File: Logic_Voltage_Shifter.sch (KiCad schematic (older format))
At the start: 5 parts, among them U5 TXB0104

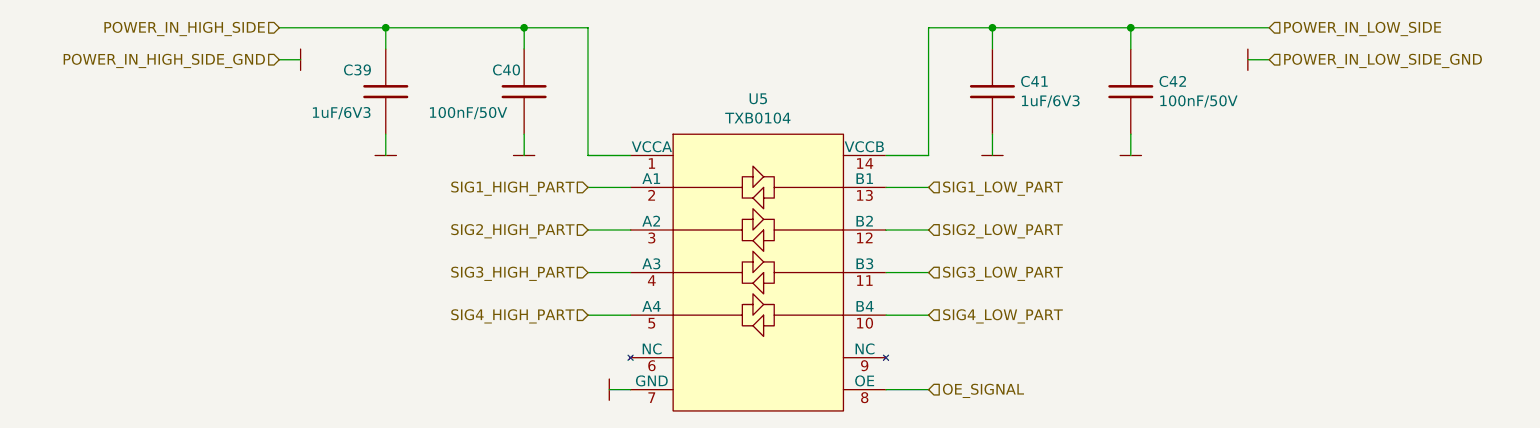
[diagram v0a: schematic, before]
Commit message: Continue connections on schematic
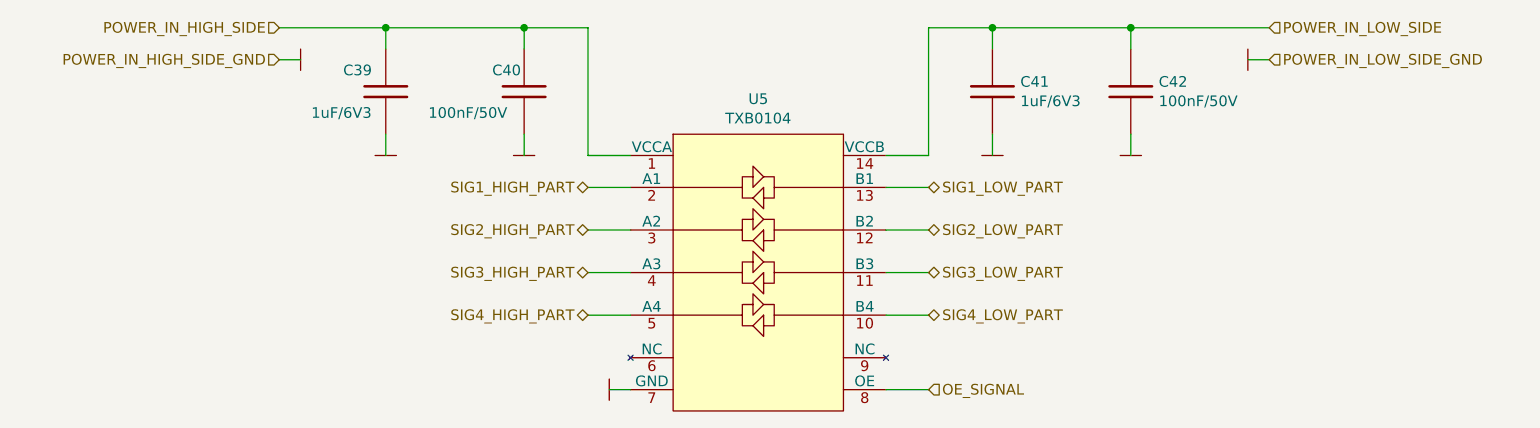
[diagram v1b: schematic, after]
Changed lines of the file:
@@
 Text HLabel 8900 6350 2    50   Input ~ 0
 OE_SIGNAL
-Text HLabel 8900 5400 2    50   Input ~ 0
+Text HLabel 8900 5400 2    50   BiDi ~ 0
 SIG1_LOW_PART
-Text HLabel 8900 5600 2    50   Input ~ 0
+Text HLabel 8900 5600 2    50   BiDi ~ 0
 SIG2_LOW_PART
-Text HLabel 8900 5800 2    50   Input ~ 0
+Text HLabel 8900 5800 2    50   BiDi ~ 0
 SIG3_LOW_PART
-Text HLabel 8900 6000 2    50   Input ~ 0
+Text HLabel 8900 6000 2    50   BiDi ~ 0
 SIG4_LOW_PART
 Wire Wire Line
@@
 Wire Wire Line
 	7500 6000 7300 6000
-Text HLabel 7300 6000 0    50   Input ~ 0
+Text HLabel 7300 6000 0    50   BiDi ~ 0
 SIG4_HIGH_PART
-Text HLabel 7300 5800 0    50   Input ~ 0
+Text HLabel 7300 5800 0    50   BiDi ~ 0
 SIG3_HIGH_PART
-Text HLabel 7300 5600 0    50   Input ~ 0
+Text HLabel 7300 5600 0    50   BiDi ~ 0
 SIG2_HIGH_PART
-Text HLabel 7300 5400 0    50   Input ~ 0
+Text HLabel 7300 5400 0    50   BiDi ~ 0
 SIG1_HIGH_PART
 $EndSCHEMATC
